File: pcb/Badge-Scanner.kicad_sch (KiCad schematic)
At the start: 32 parts, among them J3 NFC-Module, J4 I2C, J4 Micro_SD_Card_Det1, J5 Buzzer, Q1 2N7002, Q2 2N7002, Q3 AO3400A, U1 Pico W, U2 DS3231MZ

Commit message: fix: part numbers for connectors
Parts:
- J3: LCSC C157914 -> C2908606
- J4: LCSC C157926 -> C2321
- J5: LCSC C173752 -> C2319
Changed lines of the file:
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@@
 			)
 		)
-		(property "LCSC" "C173752"
+		(property "LCSC" "C2319"
 			(at 152.4 125.73 0)
 			(effects
@@
 			)
 		)
-		(property "LCSC" "C157914"
+		(property "LCSC" "C2908606"
 			(at 96.52 133.35 0)
 			(effects
@@
 			)
 		)
-		(property "LCSC" "C157926"
+		(property "LCSC" "C2321"
 			(at 115.57 55.88 0)
 			(effects

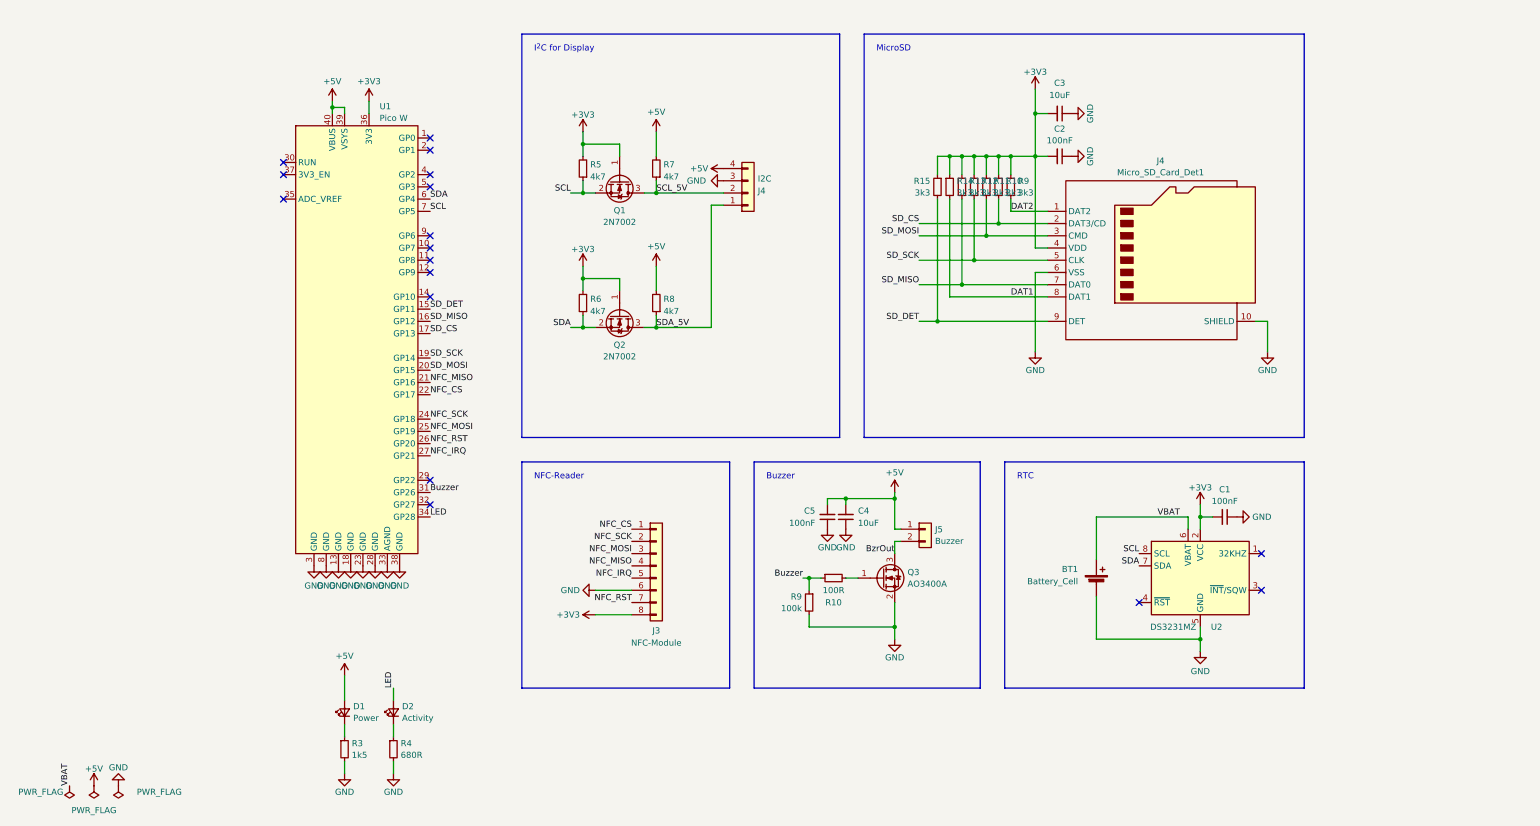
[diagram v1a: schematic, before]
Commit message: feat: add LiPo Circuitry
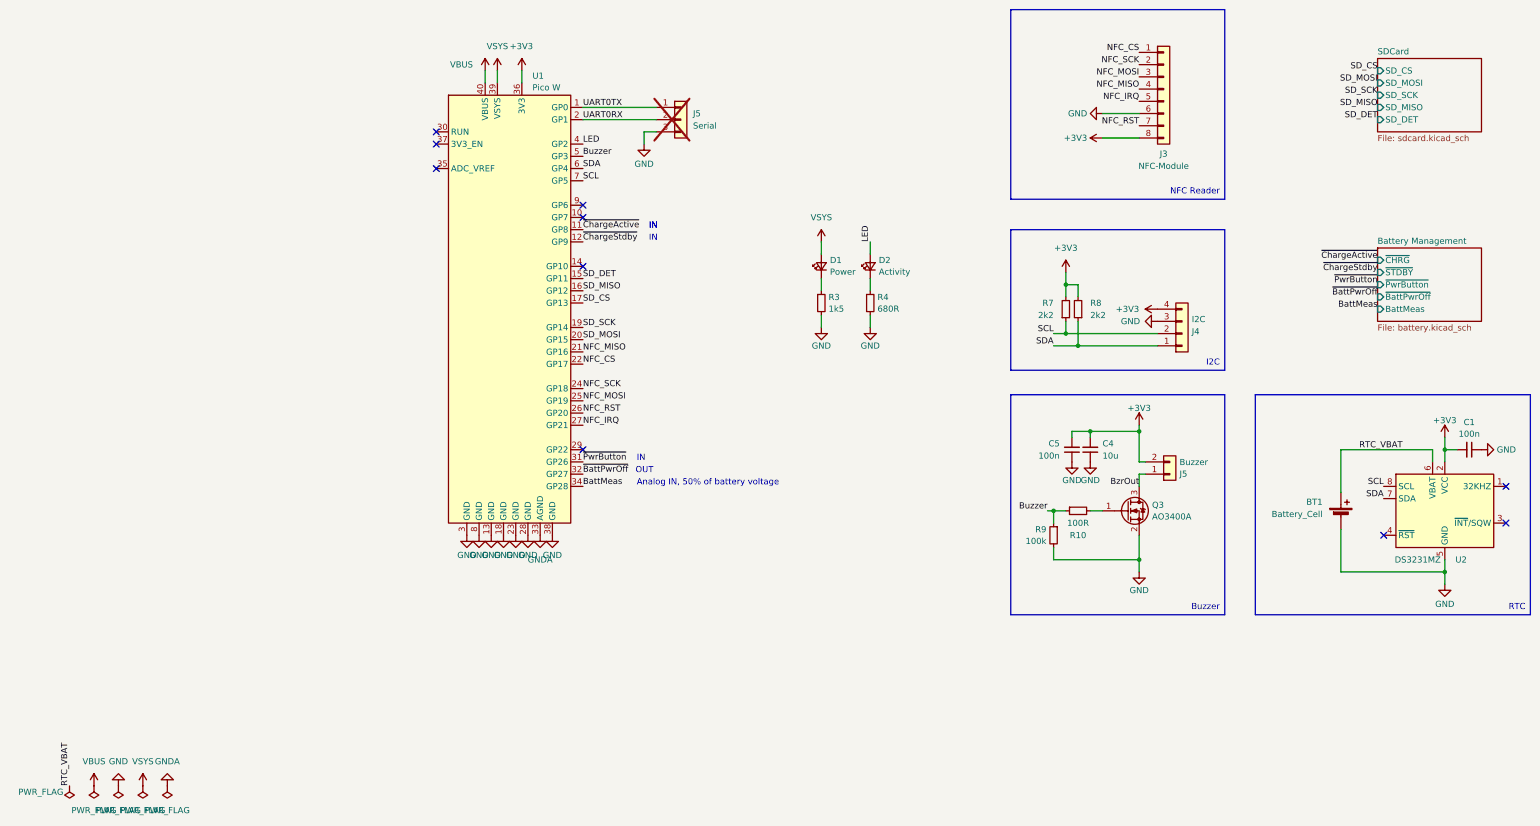
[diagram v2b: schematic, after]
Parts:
- removed C2: 100nF, Capacitor_SMD:C_0402_1005Metric, symbol Device:C_Small
- removed C3: 10uF, Capacitor_SMD:C_0402_1005Metric, symbol Device:C_Small
- removed J4: Micro_SD_Card_Det1, My_Footprints:TF_PUSH_Micro-SD-Connector, symbol Connector:Micro_SD_Card_Det1
- removed Q1, Q2: 2N7002, Package_TO_SOT_SMD:SOT-23, symbol Transistor_FET:2N7002
- removed R10, R11, R12, R13, R14, R15, R9: 3k3, Resistor_SMD:R_0402_1005Metric, symbol Device:R_Small
- removed R5, R6: 4k7, Resistor_SMD:R_0402_1005Metric, symbol Device:R_Small
- added J5: Serial, Connector_PinHeader_2.54mm:PinHeader_1x03_P2.54mm_Vertical, symbol Connector_Generic:Conn_01x03
- BT1: footprint Battery:BatteryHolder_Keystone_1060_1x2032 -> Connector_Molex:Molex_PicoBlade_53047-0210_1x02_P1.25mm_Vertical; LCSC C70377 -> C114130
- C1, C5: value 100nF -> 100n
- C4: value 10uF -> 10u
- R7, R8: value 4k7 -> 2k2
- U1: LCSC (none) -> C7203003
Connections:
- net SCL_5V is gone; now on net SCL: J4.2 (Pin_2), R7.1
- net SDA_5V is gone; now on net SDA: J4.1 (Pin_1), R8.1
- net +3V3: now also C4.2, C5.2, J4.4 (Pin_4), J5.2 (Pin_2), R7.2, R8.2
- net Buzzer: now also U1.5 (GP3); no longer U1.31 (GP26)
- net BzrOut: now also J5.1 (Pin_1); no longer J5.2 (Pin_2)
- net GND: now also J5.3 (Pin_3); no longer U1.33 (AGND)
- net LED: now also U1.4 (GP2); no longer U1.34 (GP28)
- net UART0TX: now reaches U1.1 (GP0)
- net UART0TX: now also J5.1 (Pin_1)
- net ~{ChargeActive}: now reaches U1.11 (GP8)
- net ~{ChargeStdby}: now reaches U1.12 (GP9)
- net UART0RX: now reaches U1.2 (GP1)
- net UART0RX: now also J5.2 (Pin_2)
- net ~{BattPwrOff}: now reaches U1.32 (GP27)
- removed net +5V: C4.2, C5.2, D1.2 (A), J4.4 (Pin_4), J5.1 (Pin_1), R7.2, R8.2, U1.39 (VSYS), U1.40 (VBUS)
- net VBAT renamed RTC_VBAT
- new net BattMeas: U1.34 (GP28)
- new net GNDA: U1.33 (AGND)
- new net VBUS: U1.40 (VBUS)
- new net VSYS: D1.2 (A), U1.39 (VSYS)
- new net ~{PwrButton}: U1.31 (GP26)
- no-connect marks 17 -> 10
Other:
- added sheet Battery Management (battery.kicad_sch)
- added sheet SDCard (sdcard.kicad_sch)
- note added: "Analog IN, 50% of battery voltage"
- note added: "IN"
- note added: "OUT"
- note removed: "Buzzer"
- note removed: "I^{2}C for Display"
- note removed: "MicroSD"
- note removed: "NFC-Reader"
- note removed: "RTC"
- moved on the sheet: BT1, C1, C4, C5, D1, D2, J3, J4, J5, Q3, R10, R3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

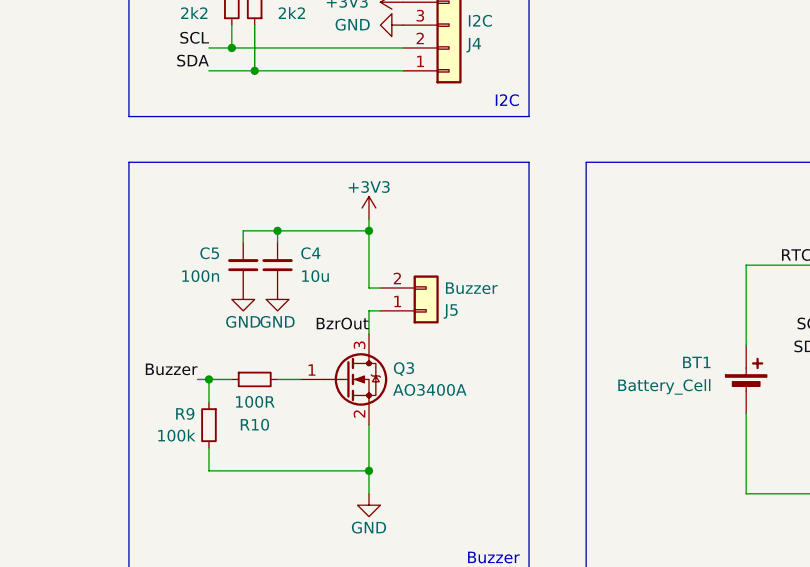
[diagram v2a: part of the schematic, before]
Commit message: fix: replace buzzer footprint
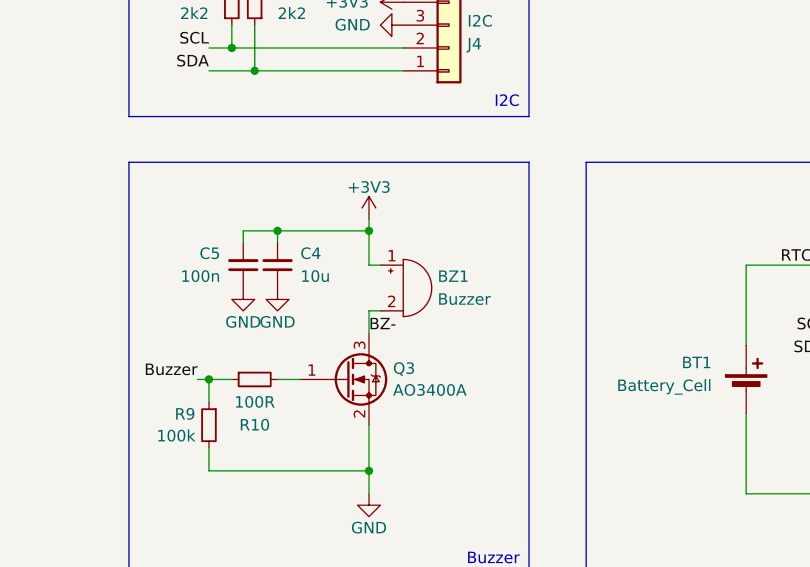
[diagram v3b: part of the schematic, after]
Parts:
- removed J5: Buzzer, Connector_JST:JST_PH_B2B-PH-K_1x02_P2.00mm_Vertical, symbol Connector_Generic:Conn_01x02
- added BZ1: Buzzer, Buzzer_Beeper:Buzzer_12x9.5RM7.6, symbol Device:Buzzer
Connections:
- net +3V3: now also BZ1.1 (+)
- net BzrOut renamed BZ-
- net BZ-: now also BZ1.2 (-)
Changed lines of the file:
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@@
-	(wire
-		(pts
-			(xy 196.85 111.76) (xy 198.12 111.76)
-		)
-		(stroke
-			(width 0)
-			(type default)
-		)
-	)
 	(wire
 		(pts
@@
 	(wire
 		(pts
-			(xy 196.85 105.41) (xy 196.85 111.76)
+			(xy 196.85 105.41) (xy 196.85 109.22)
 		)
 		(stroke
@@
 		(pts
 			(xy 189.23 44.45) (xy 196.85 44.45)
+		)
+		(stroke
+			(width 0)
+			(type default)
+		)
+	)
+	(wire
+		(pts
+			(xy 196.85 109.22) (xy 198.12 109.22)
 		)
 		(stroke
@@
 		)
 	)
-	(label "BzrOut"
-		(at 196.85 116.84 180)
-		(fields_autoplaced yes)
-		(effects
-			(font
-				(size 1.27 1.27)
-			)
-			(justify right bottom)
+	(label "BZ-"
+		(at 196.85 116.84 0)
+		(fields_autoplaced yes)
+		(effects
+			(font
+				(size 1.27 1.27)
+			)
+			(justify left bottom)
 		)
 	)
@@
 	)
 	(symbol
-		(lib_id "Connector_Generic:Conn_01x02")
-		(at 203.2 114.3 0)
-		(mirror x)
+		(lib_id "Device:Buzzer")
+		(at 200.66 111.76 0)
 		(unit 1)
 		(exclude_from_sim no)
@@
 		(on_board yes)
 		(dnp no)
-		(property "Reference" "J5"
-			(at 205.232 114.2421 0)
+		(fields_autoplaced yes)
+		(property "Reference" "BZ1"
+			(at 204.47 110.4899 0)
 			(effects
 				(font
@@
 		)
 		(property "Value" "Buzzer"
-			(at 205.232 111.8179 0)
+			(at 204.47 113.0299 0)
 			(effects
 				(font
@@
 			)
 		)
-		(property "Footprint" "Connector_JST:JST_PH_B2B-PH-K_1x02_P2.00mm_Vertical"
-			(at 203.2 114.3 0)
+		(property "Footprint" "Buzzer_Beeper:Buzzer_12x9.5RM7.6"
+			(at 200.025 109.22 90)
 			(effects
 				(font
@@
 		)
 		(property "Datasheet" "~"
-			(at 203.2 114.3 0)
-			(effects
-				(font
-					(size 1.27 1.27)
-				)
-				(hide yes)
-			)
-		)
-		(property "Description" ""
-			(at 203.2 114.3 0)
-			(effects
-				(font
-					(size 1.27 1.27)
-				)
-				(hide yes)
-			)
-		)
-		(property "LCSC" "C2319"
-			(at 203.2 114.3 0)
-			(effects
-				(font
-					(size 1.27 1.27)
-				)
-				(hide yes)
-			)
+			(at 200.025 109.22 90)
+			(effects
+				(font
+					(size 1.27 1.27)
+				)
+				(hide yes)
+			)
+		)
+		(property "Description" "Buzzer, polarized"
+			(at 200.66 111.76 0)
+			(effects
+				(font
+					(size 1.27 1.27)
+				)
+				(hide yes)
+			)
+		)
+		(pin "2"
 		)
 		(pin "1"
 		)
-		(pin "2"
-		)
 		(instances
-			(project "badge-scanner"
-				(path "/6d110148-e14d-4f93-ae7d-03d7c3052bd1"
-					(reference "J5")
+			(project ""
+				(path "/e99cd76d-c117-4654-ad48-596a9e3de149"
+					(reference "BZ1")
 					(unit 1)
 				)
-			)
-			(project "Badge-Scanner"
-				(path "/e99cd76d-c117-4654-ad48-596a9e3de149"
-					(reference "J3")
-					(unit 1)
-				)

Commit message: feat: place power button on the board
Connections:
- net ~{PwrButton}: now also U1.9 (GP6); no longer U1.31 (GP26)
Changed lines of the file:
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@@
+	)
+	(no_connect
+		(at 81.28 111.76)
 	)
 	(no_connect
@@
 	(no_connect
 		(at 50.8 43.18)
-	)
-	(no_connect
-		(at 81.28 58.42)
 	)
 	(no_connect
@@
 	(text "IN"
 		(exclude_from_sim no)
-		(at 92.456 110.998 0)
+		(at 92.456 57.658 0)
 		(effects
 			(font
@@
 	)
 	(label "~{PwrButton}"
-		(at 81.28 111.76 0)
-		(fields_autoplaced yes)
-		(effects
+		(at 81.28 58.42 0)
+		(fields_autoplaced yes)
+		(effects

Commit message: fix: add FET to measurement circuit
Disable the battery measurement circuit when the device is switched off to save energy
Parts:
- renumbered C5 to C1, C4 to C2, C1 to C3, J5 to J2
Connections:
- net BattMeas renamed BattVolt
- net ~{PwrButton} renamed ~{Button}
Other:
- sheet Battery Management ports: added BattVolt, ~{Button}; removed BattMeas, ~{PwrButton}

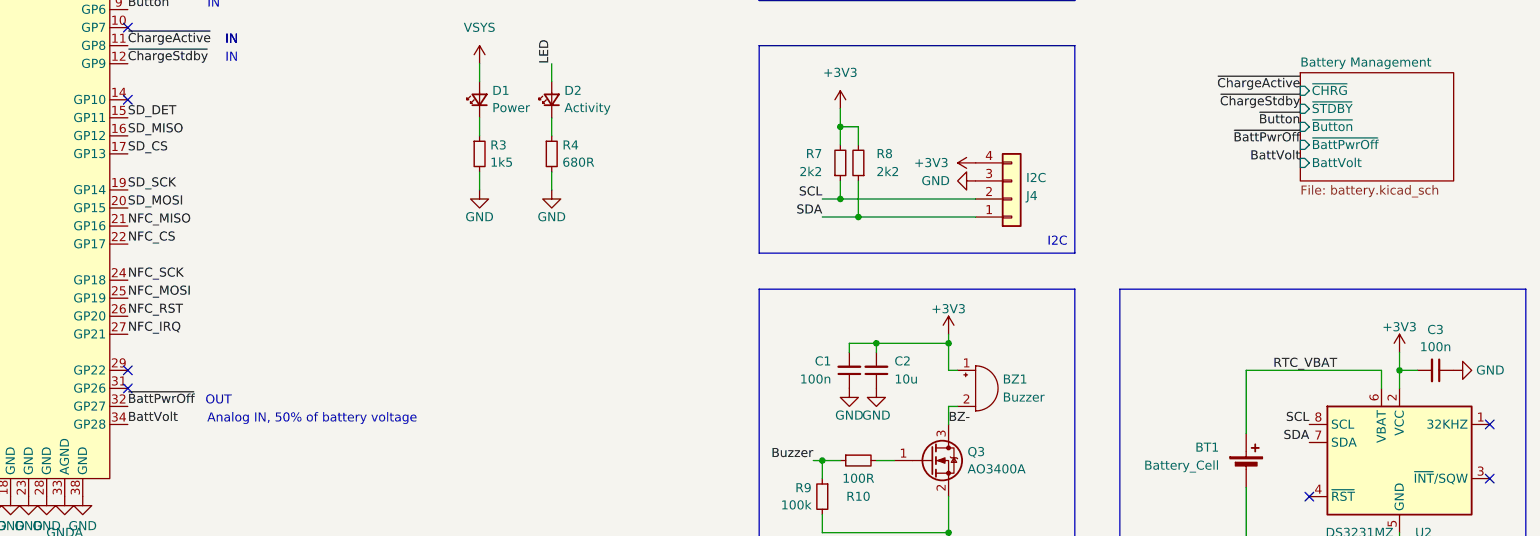
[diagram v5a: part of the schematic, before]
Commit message: fix: power switch circuit capacitance
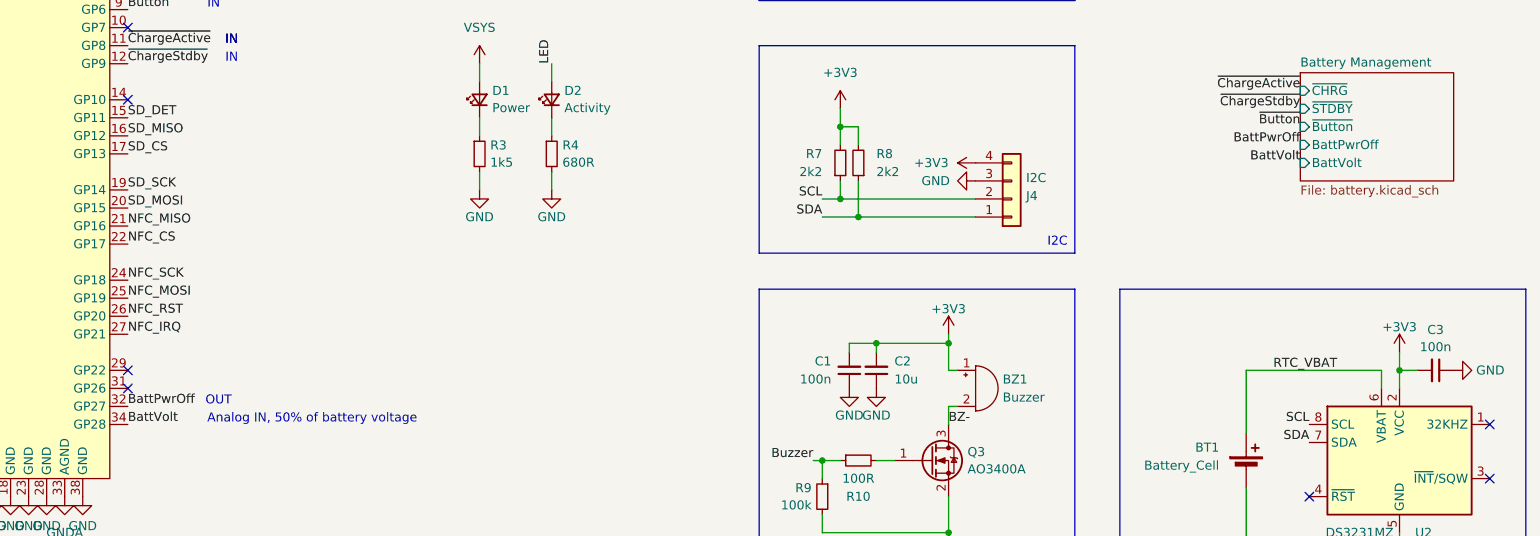
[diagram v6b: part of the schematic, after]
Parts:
- BZ1: LCSC (none) -> C252938
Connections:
- net ~{BattPwrOff} renamed BattPwrOff
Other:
- sheet Battery Management ports: added BattPwrOff; removed ~{BattPwrOff}
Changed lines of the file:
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@@
 		)
 	)
-	(label "~{BattPwrOff}"
+	(label "BattPwrOff"
 		(at 81.28 114.3 0)
 		(fields_autoplaced yes)
@@
 		)
 	)
-	(label "~{BattPwrOff}"
+	(label "BattPwrOff"
 		(at 246.38 77.47 180)
 		(fields_autoplaced yes)
@@
 			)
 		)
+		(property "LCSC" "C252938"
+			(at 200.66 111.76 0)
+			(effects
+				(font
+					(size 1.27 1.27)
+				)
+				(hide yes)
+			)
+		)
 		(pin "2"
 		)
@@
 			)
 		)
-		(pin "~{BattPwrOff}" input
+		(pin "BattPwrOff" input
 			(at 246.38 77.47 180)
 			(effects
